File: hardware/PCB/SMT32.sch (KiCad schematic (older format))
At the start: 22 parts, among them J1 USB_B_Micro, SW1 SW_DIP_x01, U1 STM32F303CCTx, U4 LD3985M33R, Y1 YSX530GA

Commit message: clear all the traces
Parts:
- added C24, C25, C26, C27: 100nF, Capacitor_SMD:C_0603_1608Metric, symbol Device:C
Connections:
- net +3V3: now also C24.1, C25.1, C26.1, C27.1
- net GND: now also C24.2, C25.2, C26.2, C27.2
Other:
- moved on the sheet: C17, C18, C19, C20, D96, J1, R25, R26, R27, U4

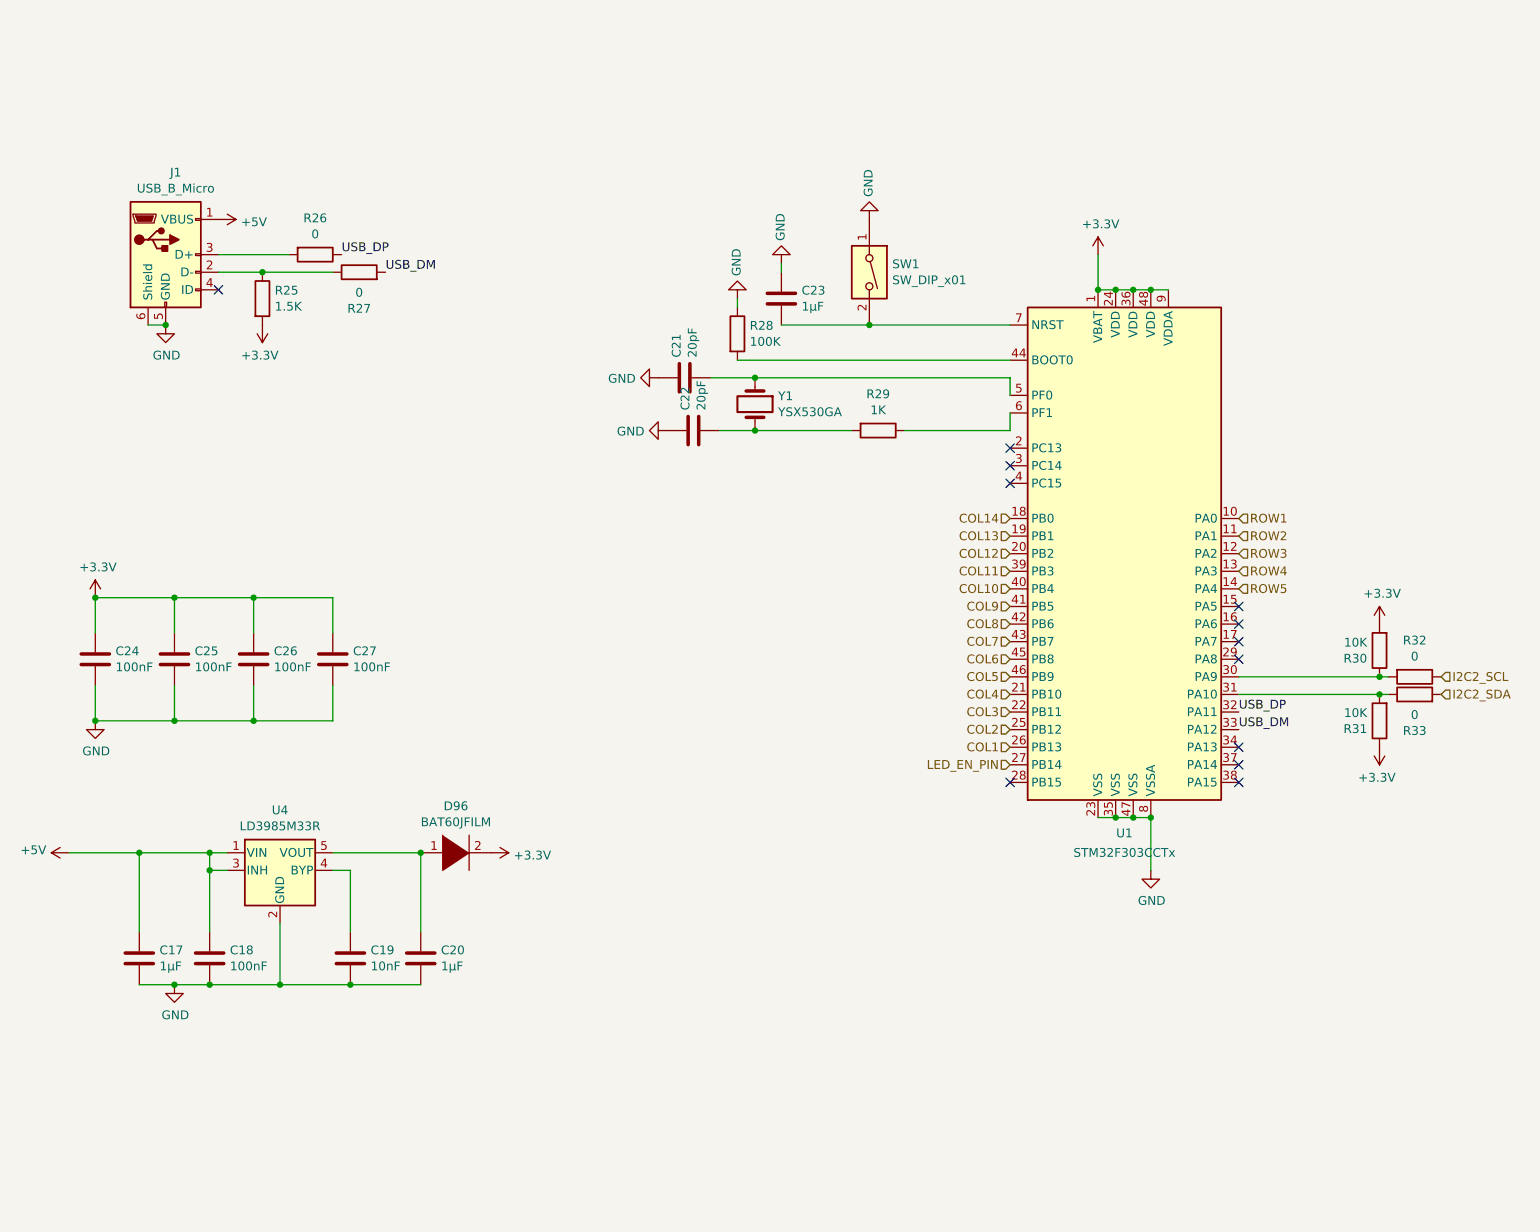
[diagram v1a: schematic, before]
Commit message: PSU placed
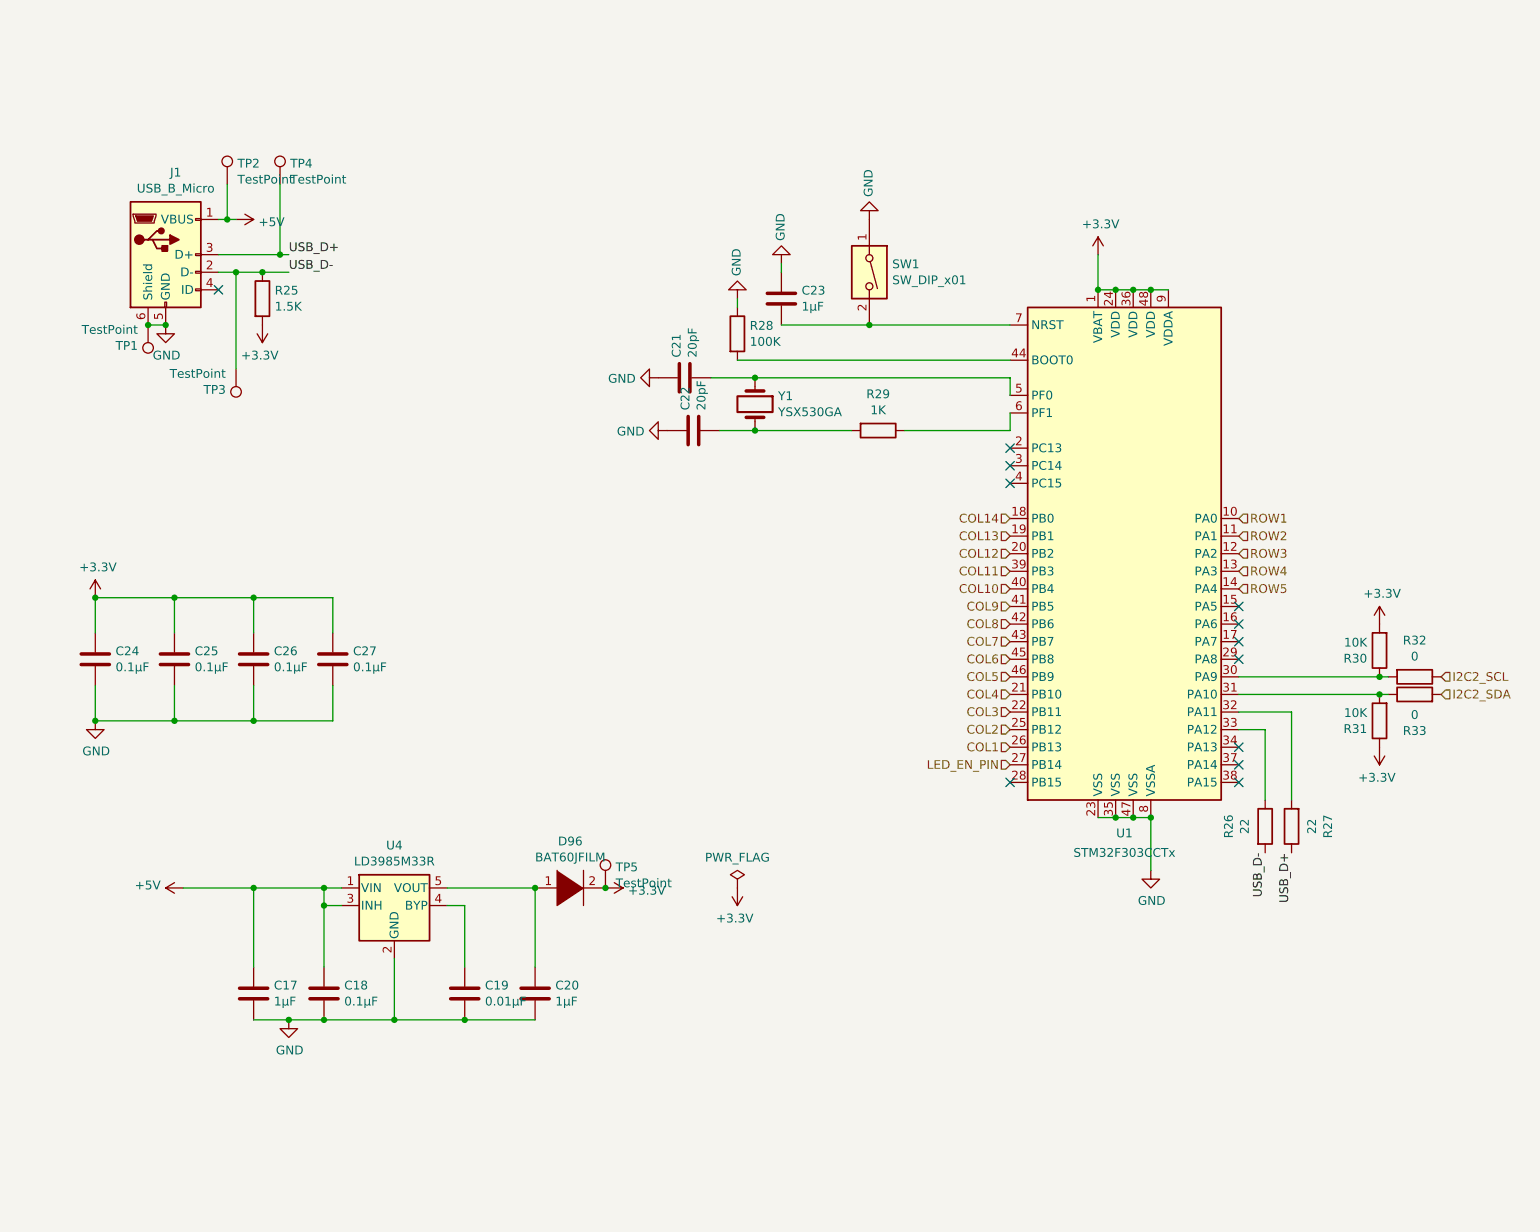
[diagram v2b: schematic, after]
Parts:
- added TP1, TP2, TP3, TP4, TP5: TestPoint, TestPoint:TestPoint_Pad_D1.0mm, symbol Connector:TestPoint
- C17, C20, C21, C22, C23: footprint Capacitor_SMD:C_0603_1608Metric -> Capacitor_SMD:C_0402_1005Metric
- C18, C24, C25, C26, C27: value 100nF -> 0.1μF; footprint Capacitor_SMD:C_0603_1608Metric -> Capacitor_SMD:C_0402_1005Metric
- C19: value 10nF -> 0.01μF; footprint Capacitor_SMD:C_0603_1608Metric -> Capacitor_SMD:C_0402_1005Metric
- R25, R28, R29, R30, R31, R32, R33: footprint Resistor_SMD:R_0603_1608Metric -> Resistor_SMD:R_0402_1005Metric
- R26, R27: value 0 -> 22; footprint Resistor_SMD:R_0603_1608Metric -> Resistor_SMD:R_0402_1005Metric
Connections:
- net +3V3: now also TP5.1
- net +5V: now also TP2.1
- net GND: now also TP1.1
- net USB_D-: now reaches J1.2 (D-), R25.1
- net USB_D-: now also R26.2, TP3.1; no longer R27.1
- net USB_D+: now reaches J1.3 (D+)
- net USB_D+: now also R27.1, TP4.1; no longer R26.2
- net USB_DM: no longer names the net of R27.2
- net USB_DM: now also U1.32 (PA11); no longer U1.33 (PA12)
- net USB_DP: no longer names the net of R26.1
- net USB_DP: now also U1.33 (PA12); no longer U1.32 (PA11)
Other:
- moved on the sheet: C17, C18, C19, C20, D96, R26, R27, U4

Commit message: PCB is done??
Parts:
- removed TP3, TP4: TestPoint, TestPoint:TestPoint_Pad_D1.0mm, symbol Connector:TestPoint
- SW1: footprint Button_Switch_SMD:SW_SPST_EVQPE1 -> Button_Switch_SMD:SW_SPST_B3U-1000P
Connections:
- net COL1: now also U1.22 (PB11); no longer U1.26 (PB13)
- net COL10: now also U1.16 (PA6); no longer U1.40 (PB4)
- net COL11: now also U1.17 (PA7); no longer U1.39 (PB3)
- net COL12: now also U1.18 (PB0); no longer U1.20 (PB2)
- net COL14: now also U1.20 (PB2); no longer U1.18 (PB0)
- net COL2: now also U1.21 (PB10); no longer U1.25 (PB12)
- net COL3: now also U1.46 (PB9); no longer U1.22 (PB11)
- net COL4: now also U1.10 (PA0); no longer U1.21 (PB10)
- net COL5: now also U1.11 (PA1); no longer U1.46 (PB9)
- net COL6: now also U1.12 (PA2); no longer U1.45 (PB8)
- net COL7: now also U1.13 (PA3); no longer U1.43 (PB7)
- net COL8: now also U1.14 (PA4); no longer U1.42 (PB6)
- net COL9: now also U1.15 (PA5); no longer U1.41 (PB5)
- net LED_EN_PIN: now also U1.34 (PA13); no longer U1.27 (PB14)
- net ROW1: now also U1.37 (PA14); no longer U1.10 (PA0)
- net ROW2: now also U1.38 (PA15); no longer U1.11 (PA1)
- net ROW3: now also U1.39 (PB3); no longer U1.12 (PA2)
- net ROW4: now also U1.40 (PB4); no longer U1.13 (PA3)
- net ROW5: now also U1.41 (PB5); no longer U1.14 (PA4)
- net USB_D+: now also R25.1
- net USB_D-: no longer R25.1
- no-connect marks 12 -> 9
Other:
- moved on the sheet: R25
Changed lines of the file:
@@
 L Device:R R25
 U 1 1 5E1D87FC
-P 2150 2400
-F 0 "R25" H 2220 2446 50  0000 L CNN
-F 1 "1.5K" H 2220 2355 50  0000 L CNN
-F 2 "Resistor_SMD:R_0402_1005Metric" V 2080 2400 50  0001 C CNN
-F 3 "~" H 2150 2400 50  0001 C CNN
-	1    2150 2400
+P 2150 2550
+F 0 "R25" H 2220 2596 50  0000 L CNN
+F 1 "1.5K" H 2220 2505 50  0000 L CNN
+F 2 "Resistor_SMD:R_0402_1005Metric" V 2080 2550 50  0001 C CNN
+F 3 "~" H 2150 2550 50  0001 C CNN
+	1    2150 2550
 	1    0    0    -1
 $EndComp
@@
 L power:+3.3V #PWR0127
 U 1 1 5E1D94BF
-P 2150 2550
-F 0 "#PWR0127" H 2150 2400 50  0001 C CNN
-F 1 "+3.3V" H 2165 2723 50  0000 C CNN
-F 2 "" H 2150 2550 50  0001 C CNN
-F 3 "" H 2150 2550 50  0001 C CNN
-	1    2150 2550
+P 2150 2700
+F 0 "#PWR0127" H 2150 2550 50  0001 C CNN
+F 1 "+3.3V" H 2165 2873 50  0000 C CNN
+F 2 "" H 2150 2700 50  0001 C CNN
+F 3 "" H 2150 2700 50  0001 C CNN
+	1    2150 2700
 	-1   0    0    1
 $EndComp
@@
 $EndComp
 NoConn ~ 1900 2350
-Wire Wire Line
-	2150 2250 2000 2250
 $Comp
 L power:+5V #PWR0128
@@
 F 0 "SW1" V 5554 2380 50  0000 L CNN
 F 1 "SW_DIP_x01" V 5645 2380 50  0000 L CNN
-F 2 "Button_Switch_SMD:SW_SPST_EVQPE1" H 5600 2250 50  0001 C CNN
+F 2 "Button_Switch_SMD:SW_SPST_B3U-1000P" H 5600 2250 50  0001 C CNN
 F 3 "~" H 5600 2250 50  0001 C CNN
 	1    5600 2250
@@
 	-1   0    0    1
 $EndComp
-Text HLabel 6400 4950 0    50   Input ~ 0
-COL1
-Text HLabel 6400 4850 0    50   Input ~ 0
-COL2
-Text HLabel 6400 4750 0    50   Input ~ 0
+Text HLabel 6400 4550 0    50   Input ~ 0
 COL3
-Text HLabel 6400 4650 0    50   Input ~ 0
+Text HLabel 7700 3650 2    50   Input ~ 0
 COL4
-Text HLabel 6400 4550 0    50   Input ~ 0
+Text HLabel 7700 3750 2    50   Input ~ 0
 COL5
-Text HLabel 6400 4450 0    50   Input ~ 0
+Text HLabel 7700 3850 2    50   Input ~ 0
 COL6
-Text HLabel 6400 4350 0    50   Input ~ 0
+Text HLabel 7700 3950 2    50   Input ~ 0
 COL7
-Text HLabel 6400 4250 0    50   Input ~ 0
+Text HLabel 7700 4050 2    50   Input ~ 0
 COL8
-Text HLabel 6400 4150 0    50   Input ~ 0
+Text HLabel 7700 4150 2    50   Input ~ 0
 COL9
-Text HLabel 6400 4050 0    50   Input ~ 0
+Text HLabel 7700 4250 2    50   Input ~ 0
 COL10
-Text HLabel 6400 3950 0    50   Input ~ 0
+Text HLabel 7700 4350 2    50   Input ~ 0
 COL11
-Text HLabel 6400 3850 0    50   Input ~ 0
+Text HLabel 6400 3650 0    50   Input ~ 0
 COL12
 Text HLabel 6400 3750 0    50   Input ~ 0
 COL13
-Text HLabel 6400 3650 0    50   Input ~ 0
+Text HLabel 6400 3850 0    50   Input ~ 0
 COL14
-Text HLabel 7700 4050 2    50   Input ~ 0
+Text HLabel 6400 4150 0    50   Input ~ 0
 ROW5
-Text HLabel 7700 3950 2    50   Input ~ 0
+Text HLabel 6400 4050 0    50   Input ~ 0
 ROW4
-Text HLabel 7700 3850 2    50   Input ~ 0
-ROW3
-Text HLabel 7700 3750 2    50   Input ~ 0
-ROW2
-Text HLabel 7700 3650 2    50   Input ~ 0
-ROW1
-NoConn ~ 7700 4150
-NoConn ~ 7700 4250
-NoConn ~ 7700 4350
 NoConn ~ 7700 4450
 NoConn ~ 6400 5150
-NoConn ~ 7700 4950
-NoConn ~ 7700 5050
-NoConn ~ 7700 5150
-Text HLabel 6400 5050 0    50   Input ~ 0
+Text HLabel 7700 4950 2    50   Input ~ 0
 LED_EN_PIN
 Wire Wire Line
@@
 Connection ~ 1200 4100
 $Comp
-L Connector:TestPoint TP4
-U 1 1 5E1E3624
-P 2250 1750
-F 0 "TP4" H 2308 1868 50  0000 L CNN
-F 1 "TestPoint" H 2308 1777 50  0000 L CNN
-F 2 "TestPoint:TestPoint_Pad_D1.0mm" H 2450 1750 50  0001 C CNN
-F 3 "~" H 2450 1750 50  0001 C CNN
-	1    2250 1750
-	1    0    0    -1
-$EndComp
-$Comp
 L Connector:TestPoint TP2
 U 1 1 5E1E444E
@@
 	-1   0    0    1
 $EndComp
-$Comp
-L Connector:TestPoint TP3
-U 1 1 5E1E690C
-P 2000 2800
-F 0 "TP3" H 2058 2918 50  0000 L CNN
-F 1 "TestPoint" H 2058 2827 50  0000 L CNN
-F 2 "TestPoint:TestPoint_Pad_D1.0mm" H 2200 2800 50  0001 C CNN
-F 3 "~" H 2200 2800 50  0001 C CNN
-	1    2000 2800
-	-1   0    0    1
-$EndComp
 Connection ~ 1500 2550
 Wire Wire Line
-	1900 2150 2250 2150
+	1900 2150 2150 2150
 Wire Wire Line
 	1950 1750 1950 1950
@@
 Wire Wire Line
 	1950 1950 2000 1950
-Wire Wire Line
-	2250 1750 2250 2150
-Connection ~ 2250 2150
-Wire Wire Line
-	2250 2150 2300 2150
-Wire Wire Line
-	2000 2800 2000 2250
-Connection ~ 2000 2250
-Wire Wire Line
-	2000 2250 1900 2250
 $Comp
 L Connector:TestPoint TP5
@@
 	-1   0    0    1
 $EndComp
-Connection ~ 2150 2250
-Wire Wire Line
-	2150 2250 2300 2250
 Wire Wire Line
 	7700 4750 8000 4750
@@
 Wire Wire Line
 	7850 4850 7850 5250
+Text HLabel 6400 4750 0    50   Input ~ 0
+COL1
+Text HLabel 7700 5050 2    50   Input ~ 0
+ROW1
+Text HLabel 7700 5150 2    50   Input ~ 0
+ROW2
+Text HLabel 6400 3950 0    50   Input ~ 0
+ROW3
+Text HLabel 6400 4650 0    50   Input ~ 0
+COL2
+Wire Wire Line
+	2150 2400 2150 2150
+Connection ~ 2150 2150
+NoConn ~ 6400 4250
+NoConn ~ 6400 4350
+NoConn ~ 6400 4450
+Wire Wire Line
+	2150 2150 2300 2150
+Wire Wire Line
+	1900 2250 2300 2250
 $EndSCHEMATC

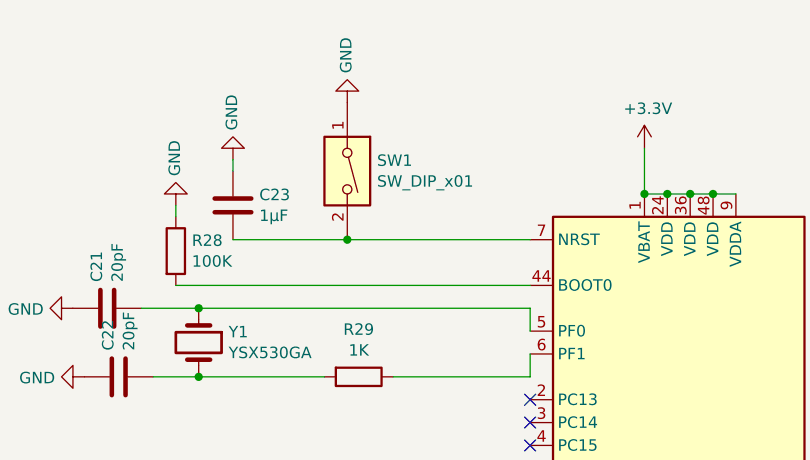
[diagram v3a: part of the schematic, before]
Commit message: making testing PCB, making sure the DFU mode is correct
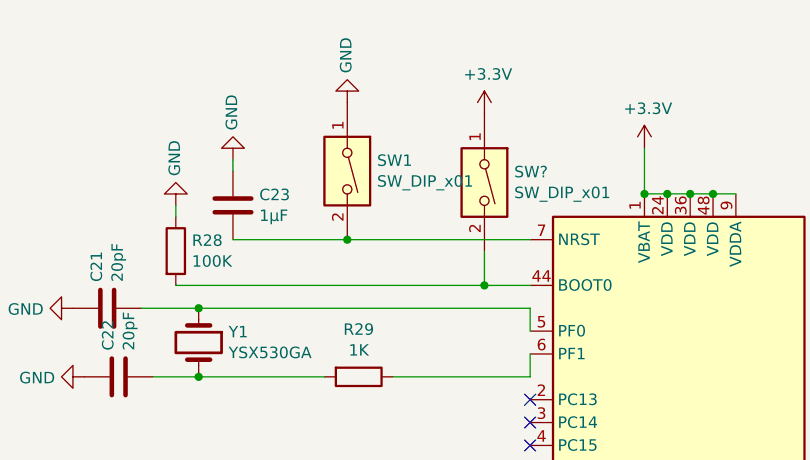
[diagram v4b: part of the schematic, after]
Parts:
- added SW?: SW_DIP_x01, Button_Switch_SMD:SW_SPST_B3U-1000P, symbol Switch:SW_DIP_x01
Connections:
- net +3V3: now also SW?.1
- net at R28.2, U1.44 (BOOT0): now also SW?.2
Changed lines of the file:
@@
 	5600 2550 6400 2550
 Connection ~ 5600 2550
-$Comp
-L Switch:SW_DIP_x01 SW1
-U 1 1 5E234436
-P 5600 2250
-F 0 "SW1" V 5554 2380 50  0000 L CNN
-F 1 "SW_DIP_x01" V 5645 2380 50  0000 L CNN
-F 2 "Button_Switch_SMD:SW_SPST_B3U-1000P" H 5600 2250 50  0001 C CNN
-F 3 "~" H 5600 2250 50  0001 C CNN
-	1    5600 2250
-	0    1    1    0
-$EndComp
 Wire Wire Line
 	5100 2550 5600 2550
@@
 $EndComp
 Wire Wire Line
-	6400 2750 4850 2750
+	6400 2750 6200 2750
 Wire Wire Line
 	4850 2400 4850 2450
@@
 Wire Wire Line
 	1900 2250 2300 2250
+$Comp
+L power:+3.3V #PWR?
+U 1 1 5E1D7BA2
+P 6200 2000
+F 0 "#PWR?" H 6200 1850 50  0001 C CNN
+F 1 "+3.3V" H 6215 2173 50  0000 C CNN
+F 2 "" H 6200 2000 50  0001 C CNN
+F 3 "" H 6200 2000 50  0001 C CNN
+	1    6200 2000
+	1    0    0    -1
+$EndComp
+$Comp
+L Switch:SW_DIP_x01 SW1
+U 1 1 5E234436
+P 5600 2250
+F 0 "SW1" V 5554 2380 50  0000 L CNN
+F 1 "SW_DIP_x01" V 5645 2380 50  0000 L CNN
+F 2 "Button_Switch_SMD:SW_SPST_B3U-1000P" H 5600 2250 50  0001 C CNN
+F 3 "~" H 5600 2250 50  0001 C CNN
+	1    5600 2250
+	0    1    1    0
+$EndComp
+$Comp
+L Switch:SW_DIP_x01 SW?
+U 1 1 5E1D944B
+P 6200 2300
+F 0 "SW?" V 6154 2430 50  0000 L CNN
+F 1 "SW_DIP_x01" V 6245 2430 50  0000 L CNN
+F 2 "Button_Switch_SMD:SW_SPST_B3U-1000P" H 6200 2300 50  0001 C CNN
+F 3 "~" H 6200 2300 50  0001 C CNN
+	1    6200 2300
+	0    1    1    0
+$EndComp
+Wire Wire Line
+	6200 2600 6200 2750
+Connection ~ 6200 2750
+Wire Wire Line
+	6200 2750 4850 2750
 $EndSCHEMATC

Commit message: Full Send, SMT assembly LOL
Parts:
- gave numbers to parts that had none: 1
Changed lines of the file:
@@
 	1900 2250 2300 2250
 $Comp
-L power:+3.3V #PWR?
+L power:+3.3V #PWR0140
 U 1 1 5E1D7BA2
 P 6200 2000
-F 0 "#PWR?" H 6200 1850 50  0001 C CNN
+F 0 "#PWR0140" H 6200 1850 50  0001 C CNN
 F 1 "+3.3V" H 6215 2173 50  0000 C CNN
 F 2 "" H 6200 2000 50  0001 C CNN
@@
 $EndComp
 $Comp
-L Switch:SW_DIP_x01 SW?
+L Switch:SW_DIP_x01 SW2
 U 1 1 5E1D944B
 P 6200 2300
-F 0 "SW?" V 6154 2430 50  0000 L CNN
+F 0 "SW2" V 6154 2430 50  0000 L CNN
 F 1 "SW_DIP_x01" V 6245 2430 50  0000 L CNN
 F 2 "Button_Switch_SMD:SW_SPST_B3U-1000P" H 6200 2300 50  0001 C CNN

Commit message: Making progress, so many distance warning!!!
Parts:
- removed C18: 0.1μF, Capacitor_SMD:C_0402_1005Metric, symbol Device:C
- removed C19: 0.01μF, Capacitor_SMD:C_0402_1005Metric, symbol Device:C
- removed C20: 1μF, Capacitor_SMD:C_0402_1005Metric, symbol Device:C
- removed D96: BAT60JFILM, Diode_SMD:D_SOD-323, symbol pspice:DIODE
- removed TP1, TP2, TP5: TestPoint, TestPoint:TestPoint_Pad_D1.0mm, symbol Connector:TestPoint
- removed U4: LD3985M33R, Package_TO_SOT_SMD:SOT-23-5, symbol Regulator_Linear:LD3985M33R_SOT23
- added C21: 22uf, Capacitor_SMD:C_0402_1005Metric, symbol Device:C
- added U3: AZ1117CH-3.3, Package_TO_SOT_SMD:SOT-223-3_TabPin2, symbol Regulator_Linear:LD1117S33TR_SOT223
- C17: value 1μF -> 10uf
- C18: renamed from C24; value 0.1μF -> 100nF
- C19: renamed from C25; value 0.1μF -> 100nF
- C20: renamed from C26; value 0.1μF -> 100nF
- C22: renamed from C27; value 0.1μF -> 100nF
- C25: renamed from C23; value 1μF -> 100nF
- Y1: value YSX530GA -> X50328MSB2GI
- renumbered C21 to C23, C22 to C24, R25 to R11, R28 to R12, R29 to R13, R26 to R14, R27 to R15, R30 to R16, R31 to R17, R32 to R18, R33 to R19, U1 to U4
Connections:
- net +3V3: now also C21.1, U3.2 (VO)
- net +5V: now also U3.3 (VI)
- net GND: now also C21.2, U3.1 (GND)
- net at U4.32 (PA11): now also R14.1; no longer R15.2
- net at U4.33 (PA12): now also R15.2; no longer R14.1
- no-connect marks 9 -> 12
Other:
- note added: "PWR"
- moved on the sheet: C18, C19, C20, C22, J1, R11
